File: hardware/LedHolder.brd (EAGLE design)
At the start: 7.6 x 12.7 mm, 3 parts

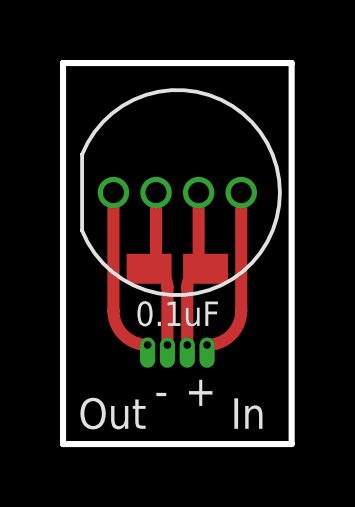
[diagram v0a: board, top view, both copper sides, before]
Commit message: Revision 2 of the latest boards
Sent these revision 2 board off to OSHPark on March 23rd, 2018. I
increased the drill sizes to accomodate the maximum of OSHPark's
+/- 2.5mil drill tolerances. I also updated the 9 branch bus to
fill top layer with 5V and move the DataIn/DataOut holes a bit to
make room for the now larger ribbon cable holes.
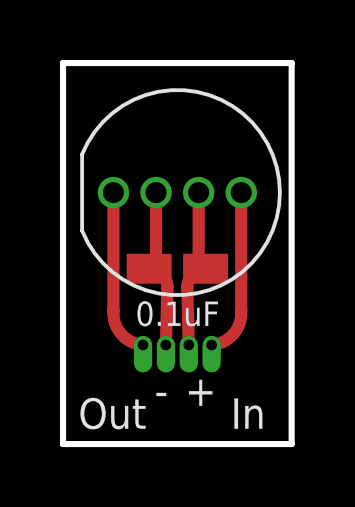
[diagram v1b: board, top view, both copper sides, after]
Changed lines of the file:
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@@
 <wire x1="3.1" y1="6.072" x2="2.87" y2="5.842" width="0.4064" layer="1" curve="-90"/>
 <wire x1="2.87" y1="5.842" x2="3.4798" y2="5.2322" width="0.4064" layer="1" curve="-90"/>
-<wire x1="3.4798" y1="5.2322" x2="3.4798" y2="3.302" width="0.4064" layer="1"/>
+<wire x1="3.4798" y1="5.2322" x2="3.429" y2="3.302" width="0.4064" layer="1"/>
 </signal>
 <signal name="S$2">
@@
 <wire x1="4.52" y1="6.072" x2="4.75" y2="5.842" width="0.4064" layer="1" curve="90"/>
 <wire x1="4.75" y1="5.842" x2="4.1402" y2="5.2322" width="0.4064" layer="1" curve="90"/>
-<wire x1="4.1402" y1="5.2322" x2="4.1402" y2="3.302" width="0.4064" layer="1"/>
+<wire x1="4.1402" y1="5.2322" x2="4.191" y2="3.302" width="0.4064" layer="1"/>
 </signal>
 <signal name="S$3">
@@
 <contactref element="E$1" pad="DATA_OUT"/>
 <wire x1="1.68" y1="8.382" x2="1.68" y2="4.4414" width="0.4064" layer="1"/>
-<wire x1="1.68" y1="4.4414" x2="2.8194" y2="3.302" width="0.4064" layer="1" curve="90"/>
+<wire x1="1.68" y1="4.4414" x2="2.667" y2="3.302" width="0.4064" layer="1" curve="90"/>
 </signal>
 <signal name="S$4">
@@
 <contactref element="E$1" pad="DATA_IN"/>
 <wire x1="5.94" y1="8.382" x2="5.94" y2="4.4414" width="0.4064" layer="1"/>
-<wire x1="5.94" y1="4.4414" x2="4.8006" y2="3.302" width="0.4064" layer="1" curve="-90"/>
+<wire x1="5.94" y1="4.4414" x2="4.953" y2="3.302" width="0.4064" layer="1" curve="-90"/>
 </signal>
 </signals>
